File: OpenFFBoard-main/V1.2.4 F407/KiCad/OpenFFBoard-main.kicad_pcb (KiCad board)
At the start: 2 copper layers, 60 x 60 mm, 64 parts, among them J1 USB4105-GF-A, SW1 TL3342F160QG/TR, SW2 TL3342F160QG/TR, U1 STM32F407VGT6, U2 TJA1051T/3, U3 LM1117, U4 USBLC6-2SC6, X1 8MHz

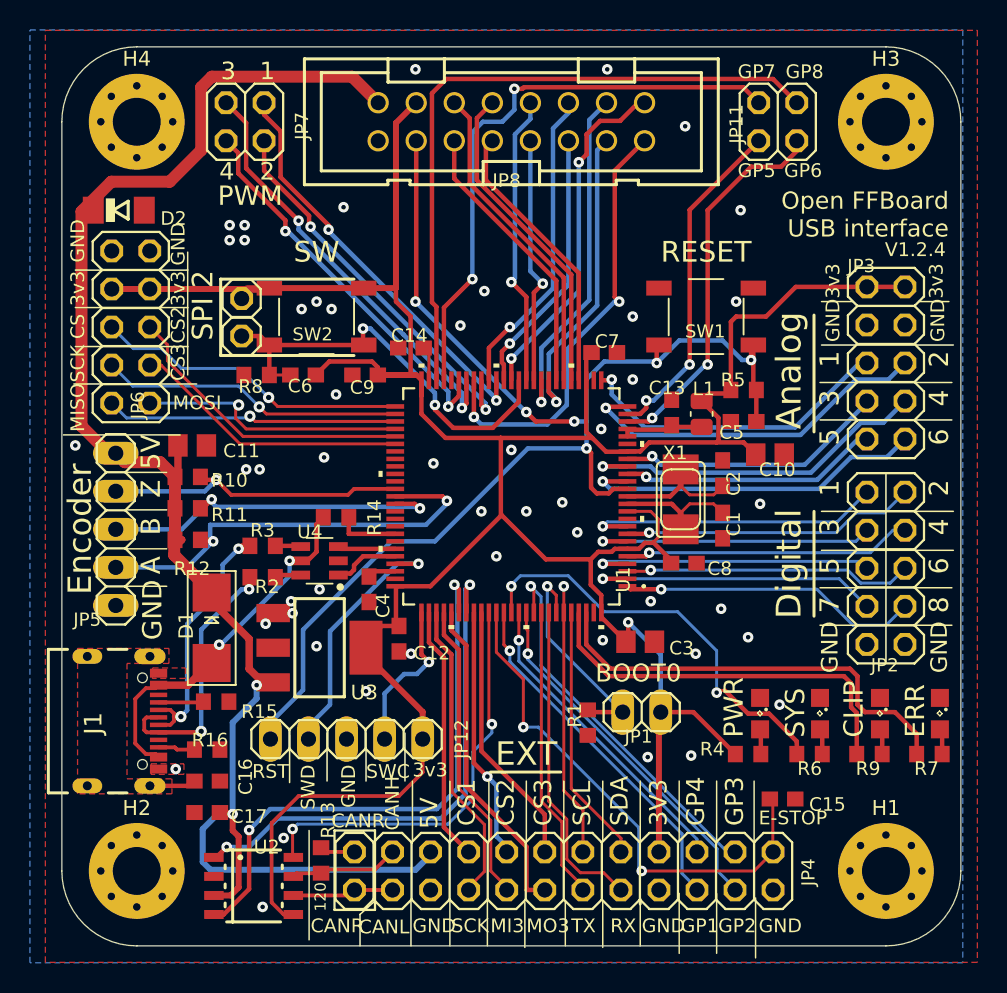
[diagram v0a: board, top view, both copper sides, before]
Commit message: Cosmetic changes on silkscreen. No more warnings
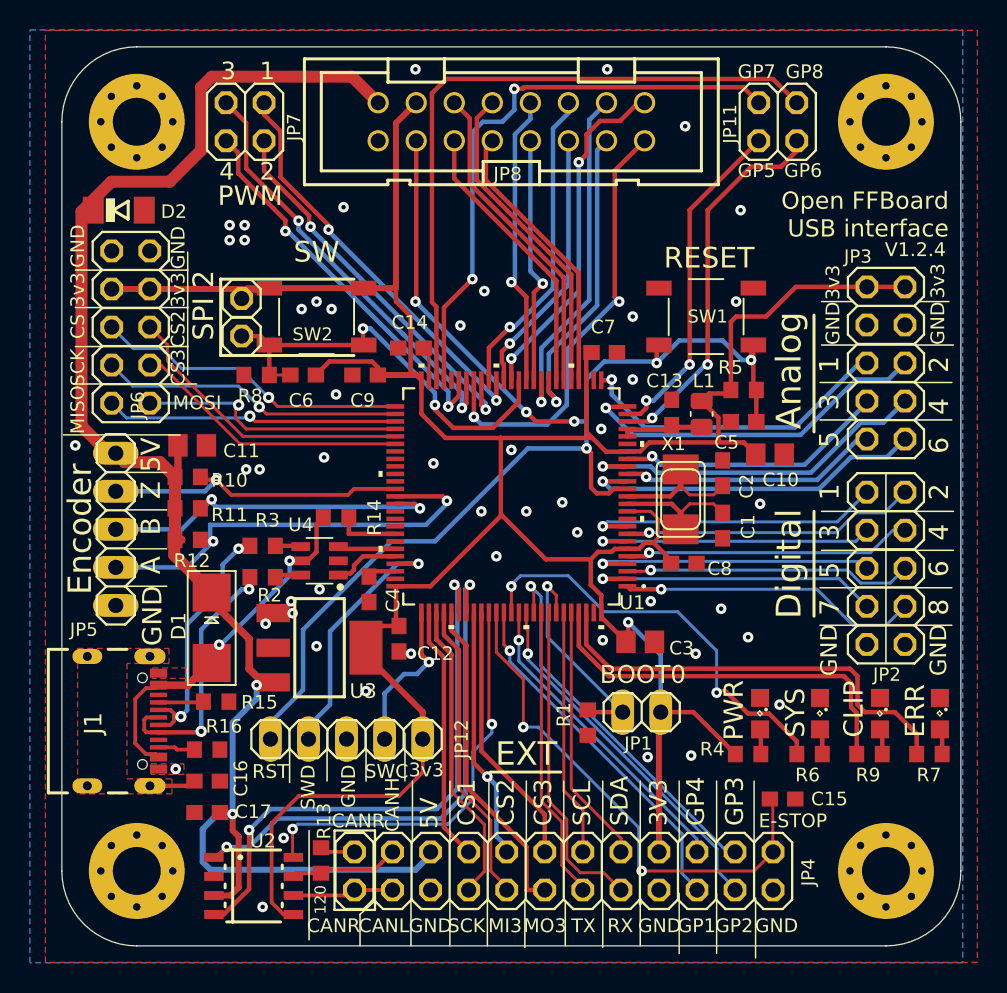
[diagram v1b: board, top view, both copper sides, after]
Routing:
- net +3.3V: track 203.9 -> 201.4 mm
- net /I2C_SCL: track 18.3 -> 16.5 mm, vias 1 -> 0
- net /NRST: track 88.4 -> 87.9 mm

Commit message: Added missing logo
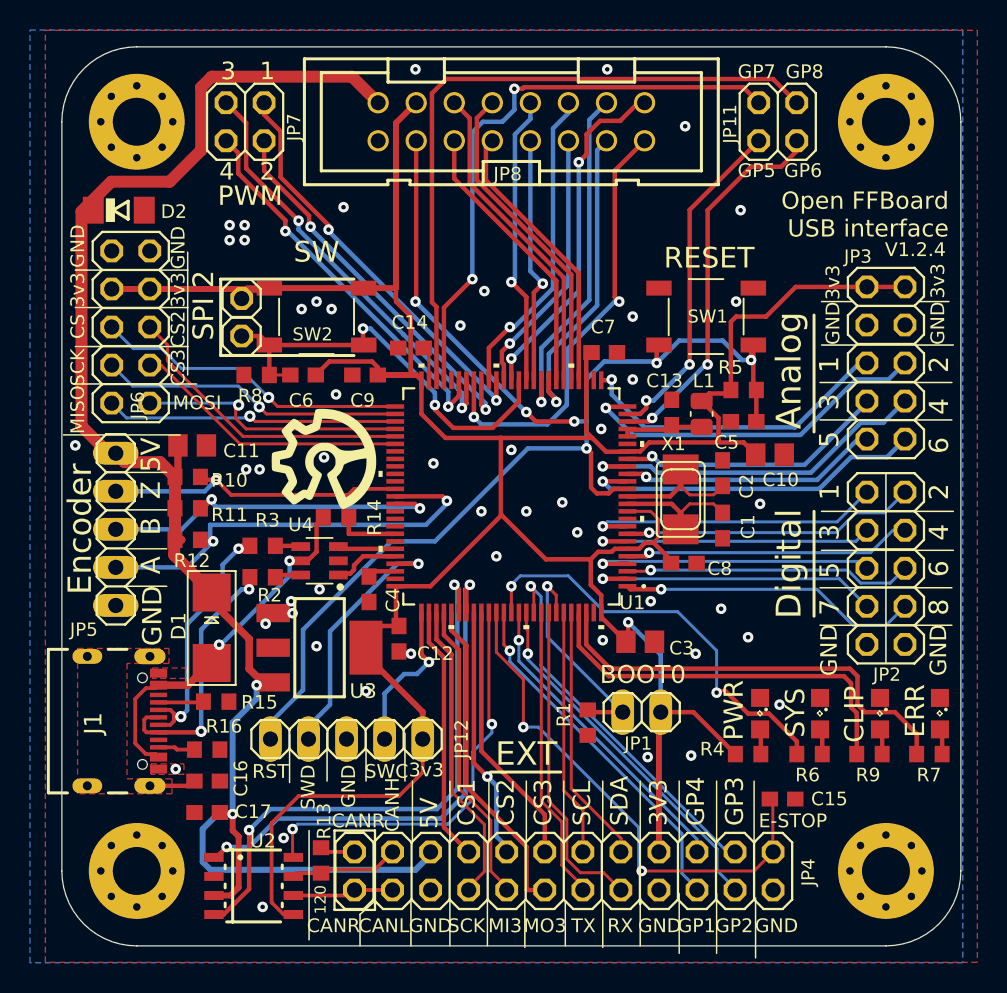
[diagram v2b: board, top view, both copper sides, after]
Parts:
- added G***: LOGO, LOGO, F.Cu at (136.0, 102.5)
- added G***: LOGO, LOGO, B.Cu at (173.5, 121.5)

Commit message: Consistent naming convention and font size on schematic
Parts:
- R1, R14, R5, R8: value 10k -> 10kR
- R10, R11, R12, R15, R16: value 5.1k -> 5.1kR
- R13: value 120 -> 120R
- R2, R3: value 22 -> 22R
- R4: value 1k -> 1kR
- R6, R7, R9: value 330 -> 330R
